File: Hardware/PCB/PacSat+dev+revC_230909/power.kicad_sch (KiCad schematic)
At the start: 67 parts, among them U206 TLP3905, U86 TPS7A7001DDA, U87 MAX1556AEBT+, U88 MAX1556A, U90 STWD100NYWY3F, U91 MAX4995ALAUT, U92 MAX4995ALAUT, U93 MAX4995ALAUT, U94 MAX4995ALAUT, U95 STWD100NYWY3F

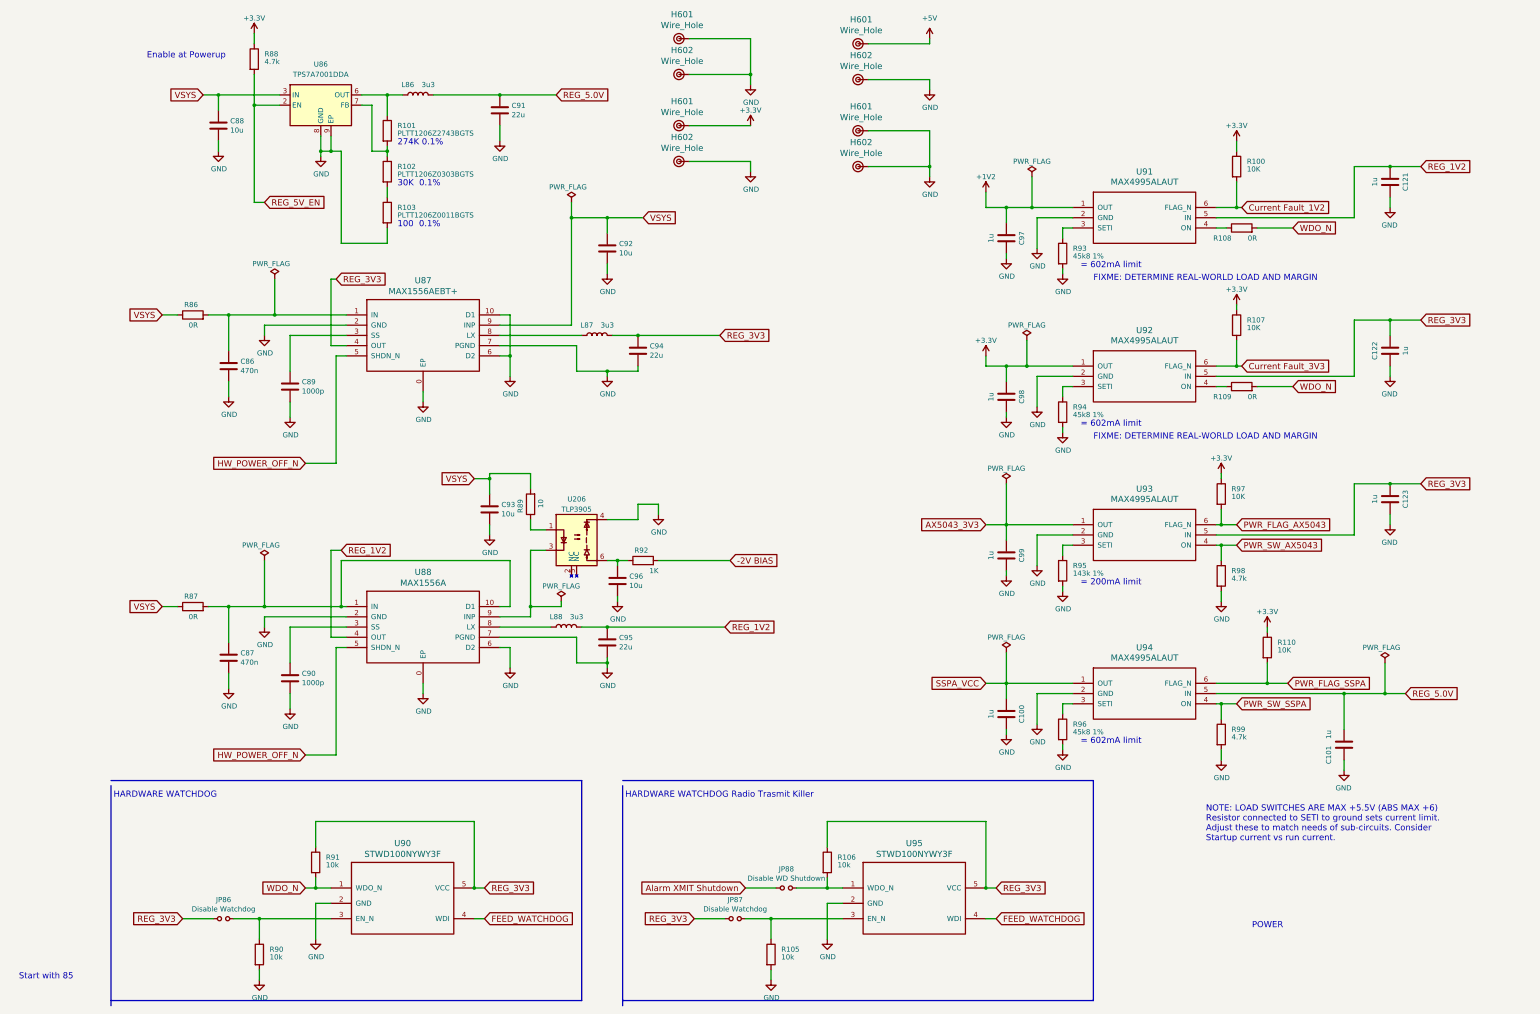
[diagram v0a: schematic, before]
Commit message: Changed schematic to add Select lines for each AX5043 on the CPU.
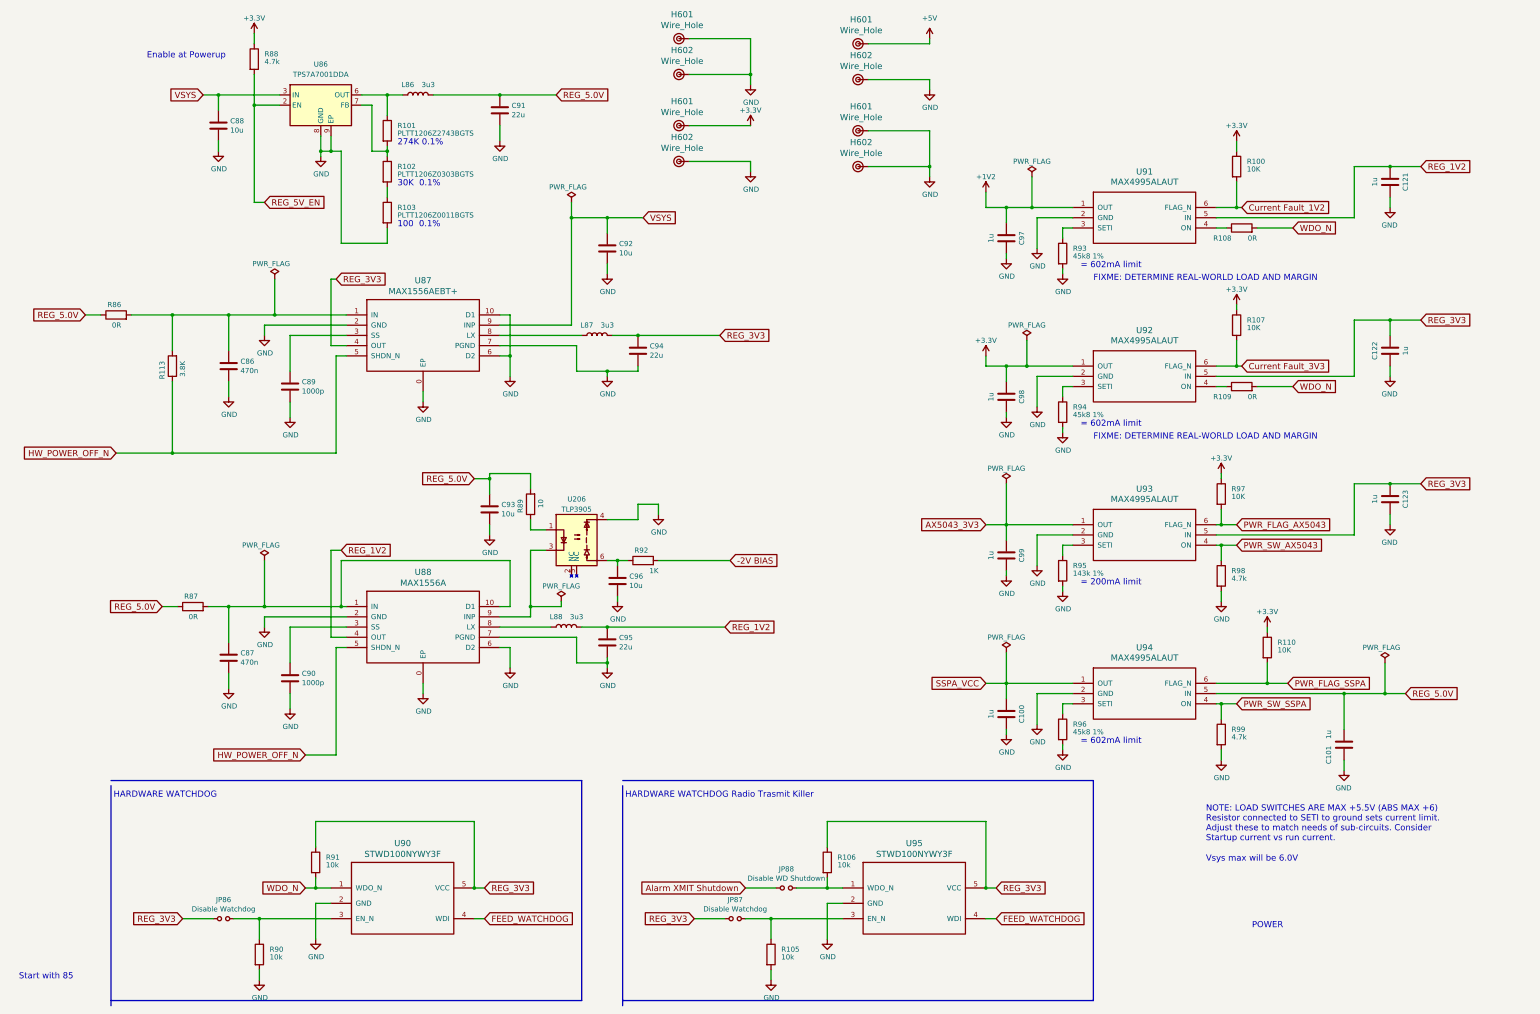
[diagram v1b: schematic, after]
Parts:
- added R113: 3.8K, Resistor_SMD:R_0603_1608Metric_Pad0.98x0.95mm_HandSolder, symbol Device:R
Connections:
- net HW_POWER_OFF_N: now also R113.1
- net REG_5.0V: now also C93.1, R86.1, R87.1, R89.2
- net VSYS: no longer C93.1, R86.1, R87.1, R89.2
- net at C86.1, R86.2, U87.1 (IN): now also R113.2
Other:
- note added: "Vsys max will be 6.0V"
- moved on the sheet: R86
